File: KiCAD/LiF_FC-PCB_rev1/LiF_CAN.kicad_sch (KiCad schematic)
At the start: 23 parts, among them J5 DE9_Socket_MountingHoles, J6 CAN Upstream, J7 CAN Upstream, J8 CAN 5V0_{EN}, J9 CAN 3V3_{EN}, SW4 CAN Termination Select, U7 MCP2542FD-E/SN

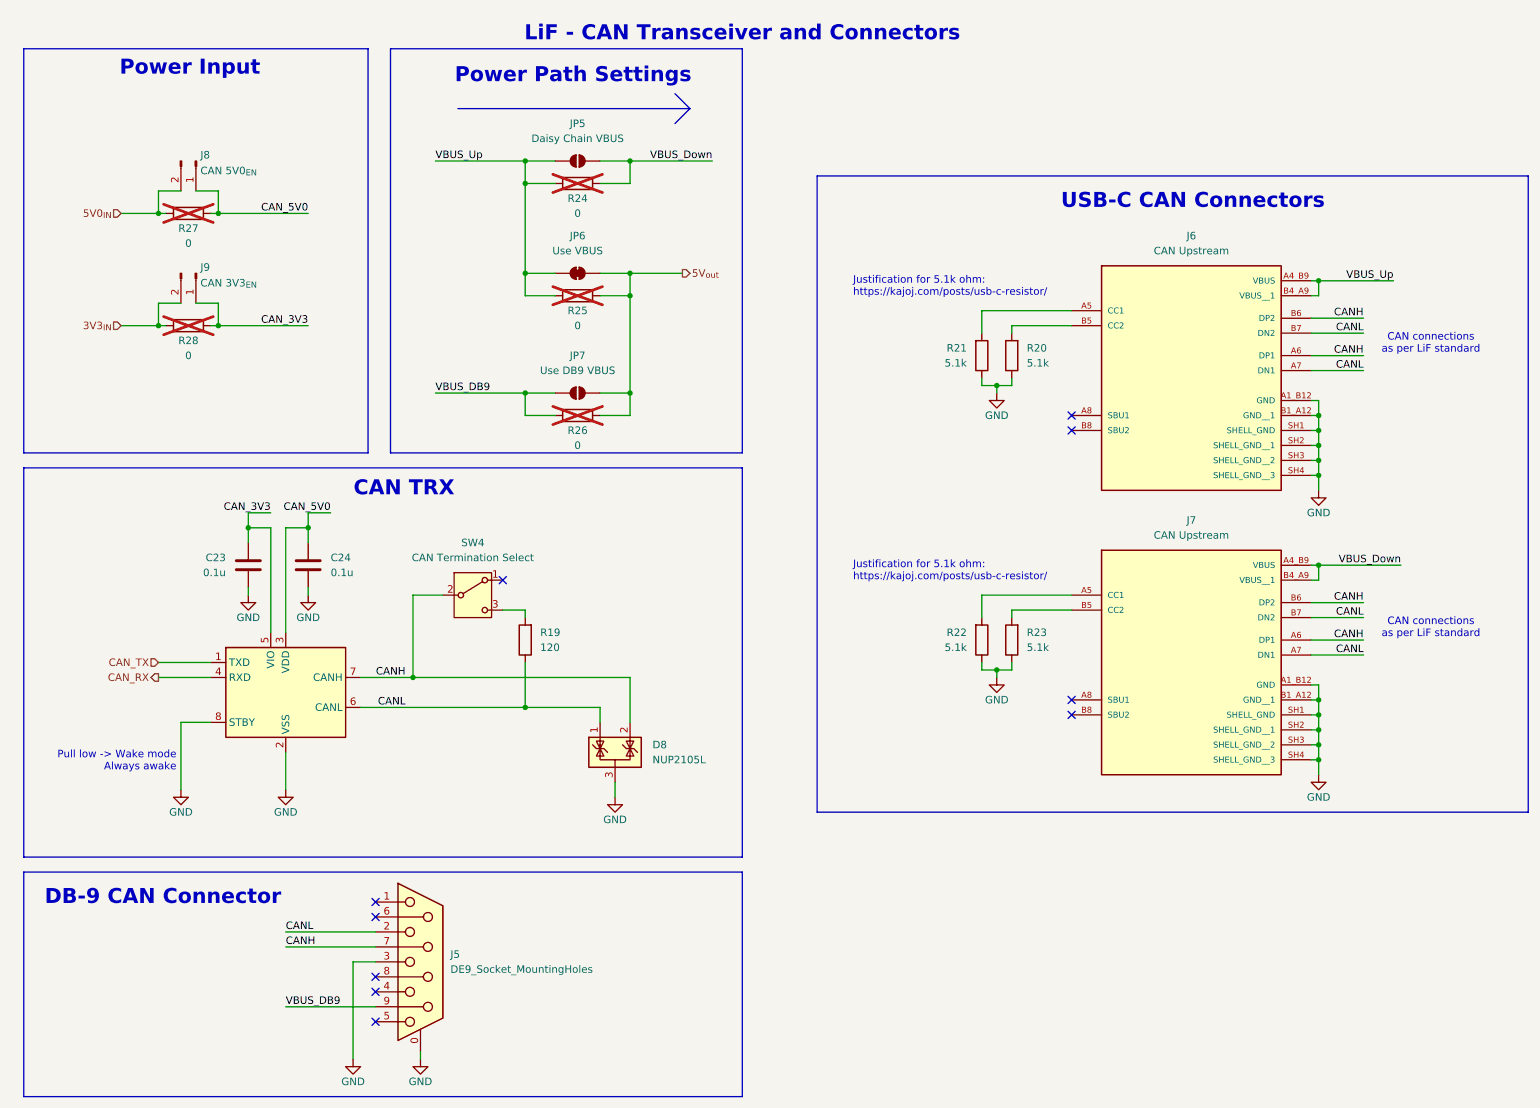
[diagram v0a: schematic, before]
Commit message: reverted 5V reg, reworked power distribution logic, swapped power OR-ing ICs
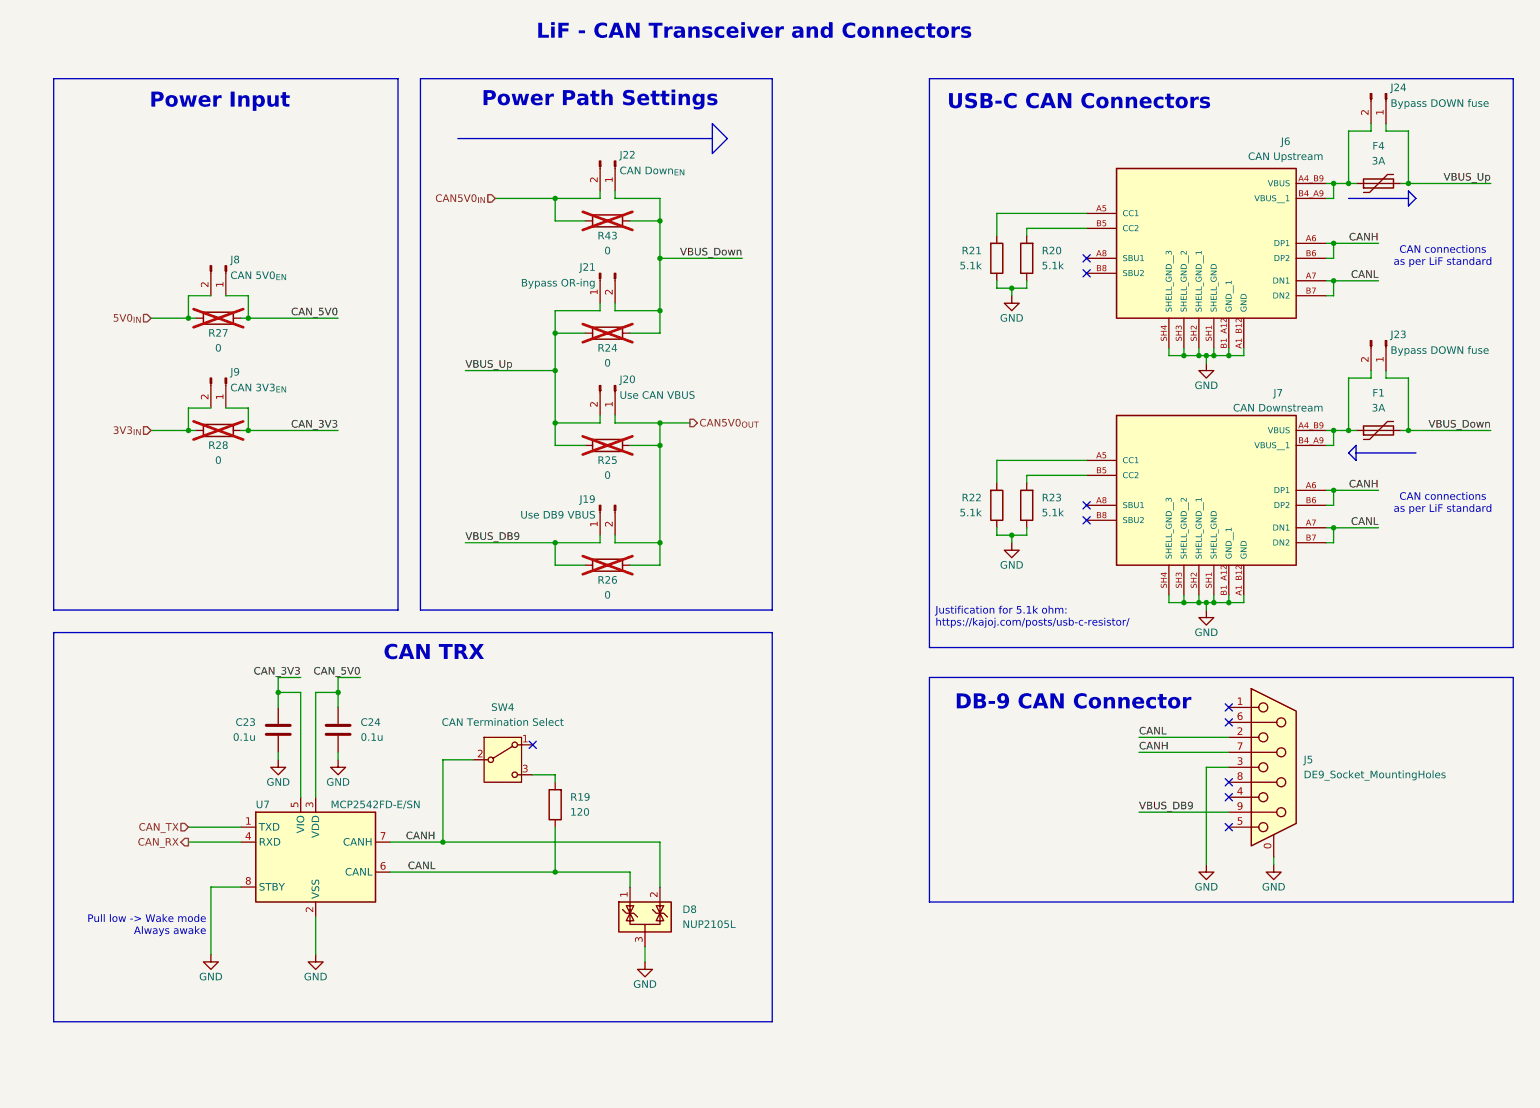
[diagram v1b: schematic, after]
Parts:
- removed JP5: Daisy Chain VBUS, Jumper:SolderJumper-2_P1.3mm_Open_RoundedPad1.0x1.5mm, symbol Jumper:SolderJumper_2_Open
- removed JP6: Use VBUS, Jumper:SolderJumper-2_P1.3mm_Open_RoundedPad1.0x1.5mm, symbol Jumper:SolderJumper_2_Bridged
- removed JP7: Use DB9 VBUS, Jumper:SolderJumper-2_P1.3mm_Open_RoundedPad1.0x1.5mm, symbol Jumper:SolderJumper_2_Open
- added F1, F4: 3A, symbol Device:Polyfuse
- added J19: Use DB9 VBUS, Connector_PinHeader_1.27mm:PinHeader_1x02_P1.27mm_Vertical, symbol Connector:Conn_01x02_Pin
- added J20: Use CAN VBUS, Connector_PinHeader_1.27mm:PinHeader_1x02_P1.27mm_Vertical, symbol Connector:Conn_01x02_Pin
- added J21: Bypass OR-ing, Connector_PinHeader_1.27mm:PinHeader_1x02_P1.27mm_Vertical, symbol Connector:Conn_01x02_Pin
- added J22: CAN Down_{EN}, Connector_PinHeader_1.27mm:PinHeader_1x02_P1.27mm_Vertical, symbol Connector:Conn_01x02_Pin
- added J23, J24: Bypass DOWN fuse, Connector_PinHeader_1.27mm:PinHeader_1x02_P1.27mm_Vertical, symbol Connector:Conn_01x02_Pin
- added R43: 0, Resistor_SMD:R_0805_2012Metric, symbol Device:R
- J7: value CAN Upstream -> CAN Downstream
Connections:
- net VBUS_DB9: now also J19.1 (Pin_1)
- net VBUS_Down: now also F1.2, J21.2 (Pin_2), J22.1 (Pin_1), J23.1 (Pin_1), R43.1; no longer J7.A4_B9 (VBUS), J7.B4_A9 (VBUS__1)
- net VBUS_Up: now also F4.2, J20.2 (Pin_2), J21.1 (Pin_1), J24.1 (Pin_1); no longer J6.A4_B9 (VBUS), J6.B4_A9 (VBUS__1)
- net 5V_{out} renamed CAN5V0_{OUT}
- net CAN5V0_{OUT}: now also J19.2 (Pin_2), J20.1 (Pin_1)
- new net: F1.1, J23.2 (Pin_2), J7.A4_B9 (VBUS), J7.B4_A9 (VBUS__1)
- new net: F4.1, J24.2 (Pin_2), J6.A4_B9 (VBUS), J6.B4_A9 (VBUS__1)
- new net CAN5V0_{IN}: J22.2 (Pin_2), R43.2
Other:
- moved on the sheet: C23, C24, D8, J5, J6, J8, J9, R19, R20, R21, R24, R25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

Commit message: Finished schematics, mostly. Only MCU sheet left. Doing component sourcing
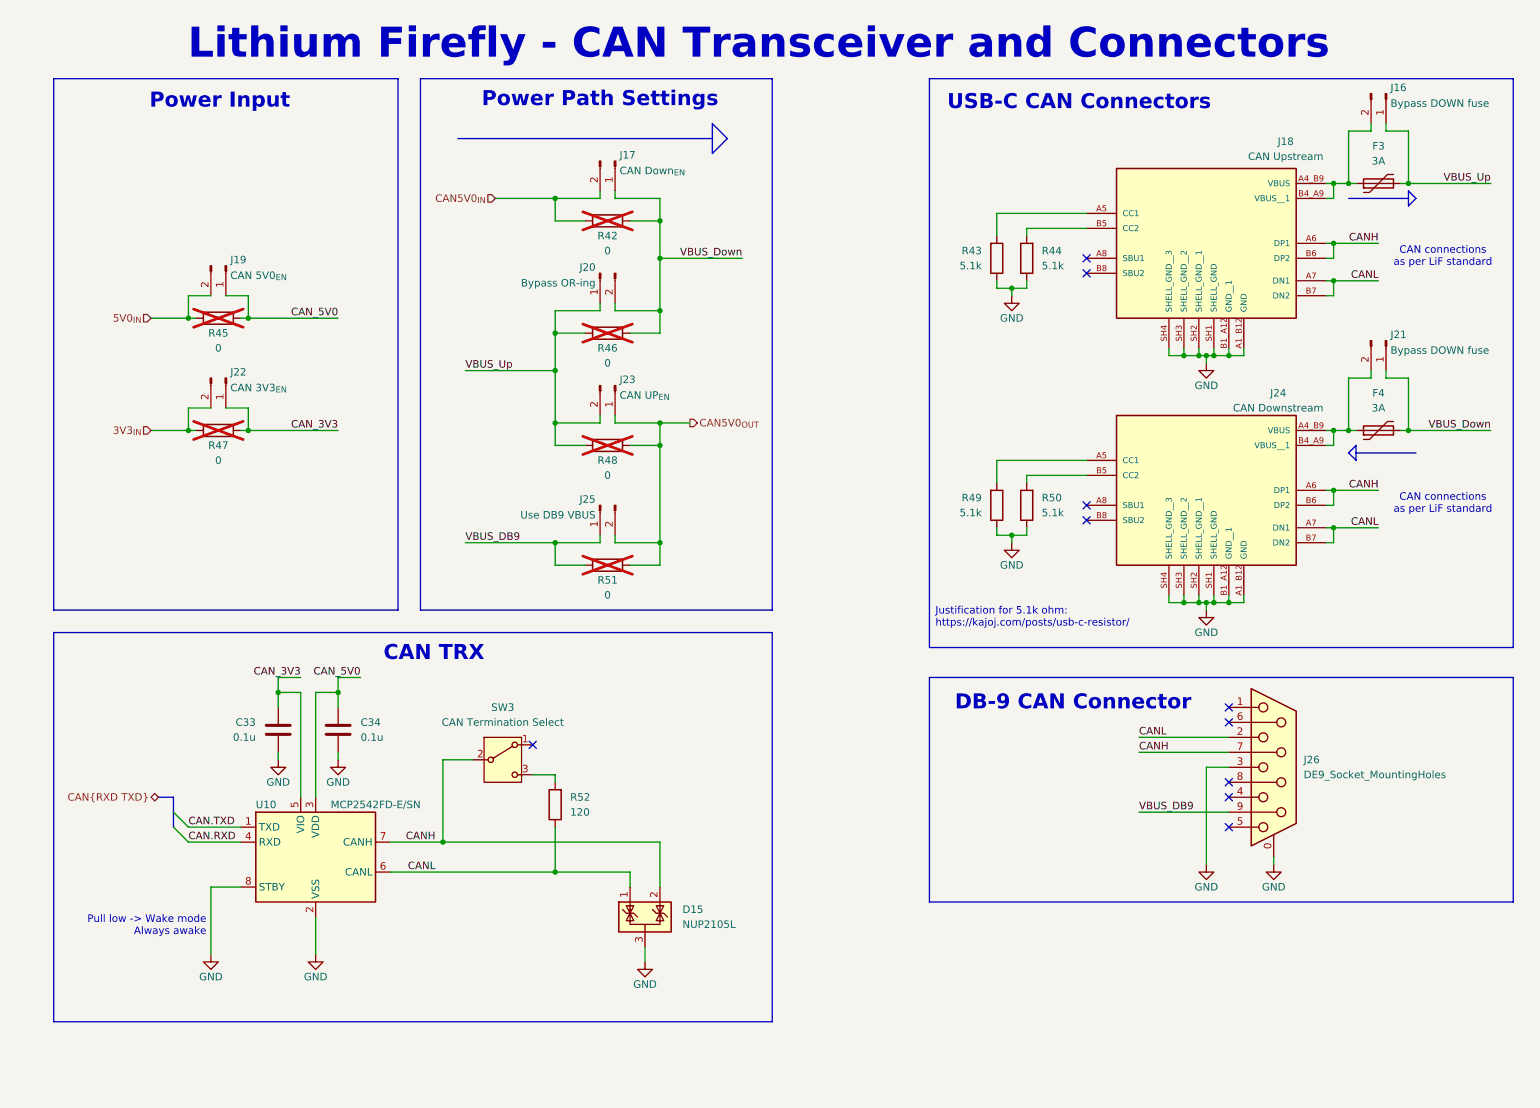
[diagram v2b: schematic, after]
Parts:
- C33: renamed from C23; DKPN (none) -> 490-12005-1-ND; PN (none) -> GRM21BR72A104KAC4L
- C34: renamed from C24; DKPN (none) -> 490-12005-1-ND; PN (none) -> GRM21BR72A104KAC4L
- F3: renamed from F4; footprint (none) -> Fuse:Fuse_0805_2012Metric; DKPN (none) -> 13-SMD1812B300TFTCT-ND; PN (none) -> SMD1812B300TFT
- F4: renamed from F1; footprint (none) -> Fuse:Fuse_0805_2012Metric; DKPN (none) -> 13-SMD1812B300TFTCT-ND; PN (none) -> SMD1812B300TFT
- J16: renamed from J24; footprint Connector_PinHeader_1.27mm:PinHeader_1x02_P1.27mm_Vertical -> Connector_PinHeader_2.54mm:PinHeader_1x02_P2.54mm_Vertical
- J17: renamed from J22; footprint Connector_PinHeader_1.27mm:PinHeader_1x02_P1.27mm_Vertical -> Connector_PinHeader_2.54mm:PinHeader_1x02_P2.54mm_Vertical
- J19: renamed from J8; footprint Connector_PinHeader_1.27mm:PinHeader_1x02_P1.27mm_Vertical -> Connector_PinHeader_2.54mm:PinHeader_1x02_P2.54mm_Vertical
- J20: renamed from J21; footprint Connector_PinHeader_1.27mm:PinHeader_1x02_P1.27mm_Vertical -> Connector_PinHeader_2.54mm:PinHeader_1x02_P2.54mm_Vertical
- J21: renamed from J23; footprint Connector_PinHeader_1.27mm:PinHeader_1x02_P1.27mm_Vertical -> Connector_PinHeader_2.54mm:PinHeader_1x02_P2.54mm_Vertical
- J22: renamed from J9; footprint Connector_PinHeader_1.27mm:PinHeader_1x02_P1.27mm_Vertical -> Connector_PinHeader_2.54mm:PinHeader_1x02_P2.54mm_Vertical
- J23: renamed from J20; value Use CAN VBUS -> CAN UP_{EN}; footprint Connector_PinHeader_1.27mm:PinHeader_1x02_P1.27mm_Vertical -> Connector_PinHeader_2.54mm:PinHeader_1x02_P2.54mm_Vertical
- J25: renamed from J19; footprint Connector_PinHeader_1.27mm:PinHeader_1x02_P1.27mm_Vertical -> Connector_PinHeader_2.54mm:PinHeader_1x02_P2.54mm_Vertical
- renumbered D8 to D15, J6 to J18, J7 to J24, J5 to J26, R43 to R42, R21 to R43, R20 to R44, R27 to R45, R24 to R46, R28 to R47, R25 to R48, R22 to R49, R23 to R50, R26 to R51, R19 to R52, SW4 to SW3, U7 to U10
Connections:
- net CAN_RX renamed CAN.RXD
- net CAN_TX renamed CAN.TXD
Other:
- note added: "Lithium Firefly - CAN Transceiver and Connectors"
- note removed: "LiF - CAN Transceiver and Connectors"
- company: (none) -> Lithium Firefly Team

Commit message: fixing ERC bugs on schematic. Only MCU left
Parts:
- added TP26: GND, TestPoint:TestPoint_Bridge_Pitch2.54mm_Drill1.0mm, symbol Connector:TestPoint
- added TP27: CANH, TestPoint:TestPoint_Bridge_Pitch2.54mm_Drill1.0mm, symbol Connector:TestPoint
- added TP28: CANL, TestPoint:TestPoint_Bridge_Pitch2.54mm_Drill1.0mm, symbol Connector:TestPoint
- U10: DKPN (none) -> MCP2542FD-E/SN-ND; PN (none) -> MCP2542FD-E/SN
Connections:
- net CANH: now also TP27.1
- net CANL: now also TP28.1
- net GND: now also TP26.1

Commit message: Added MCU pinout, shanged shift registers to GPIO expanders to save pins on MCU
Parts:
- renumbered J16 to J17, J17 to J18, J18 to J19, J19 to J20, J20 to J21, J21 to J22, J22 to J23, J23 to J24, J24 to J25, J25 to J26, J26 to J27, R42 to R43, R43 to R44, R44 to R45, R45 to R46, R46 to R47, R47 to R48, R48 to R49, R49 to R50, R50 to R51, R51 to R52, R52 to R53, TP28 to TP19, TP27 to TP20, TP26 to TP21
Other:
- title: (none) -> Lithium Firefly Custom FC/CC PCB
